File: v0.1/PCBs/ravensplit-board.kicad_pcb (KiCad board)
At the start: 2 copper layers, 131.3 x 100.3 mm, 47 parts

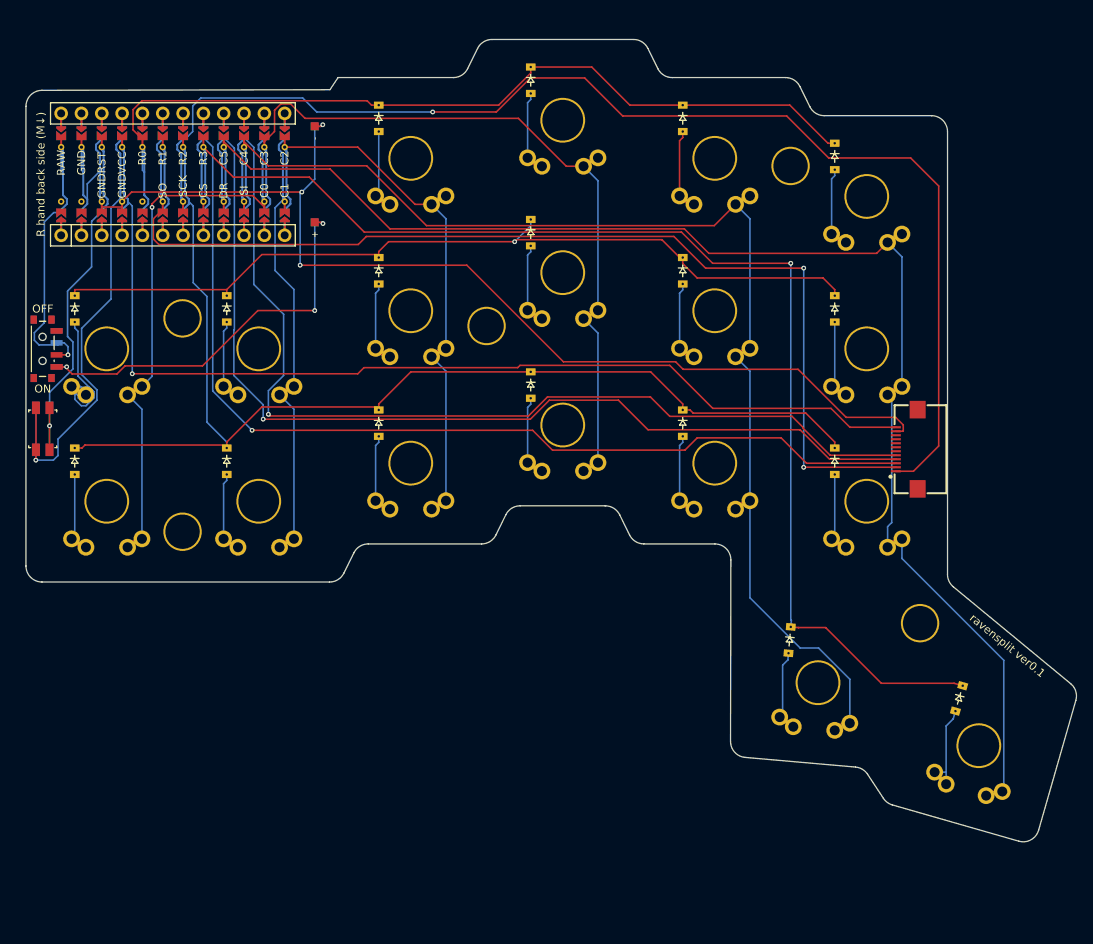
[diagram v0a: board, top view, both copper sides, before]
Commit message: Center MCU better and auto redo PCBs
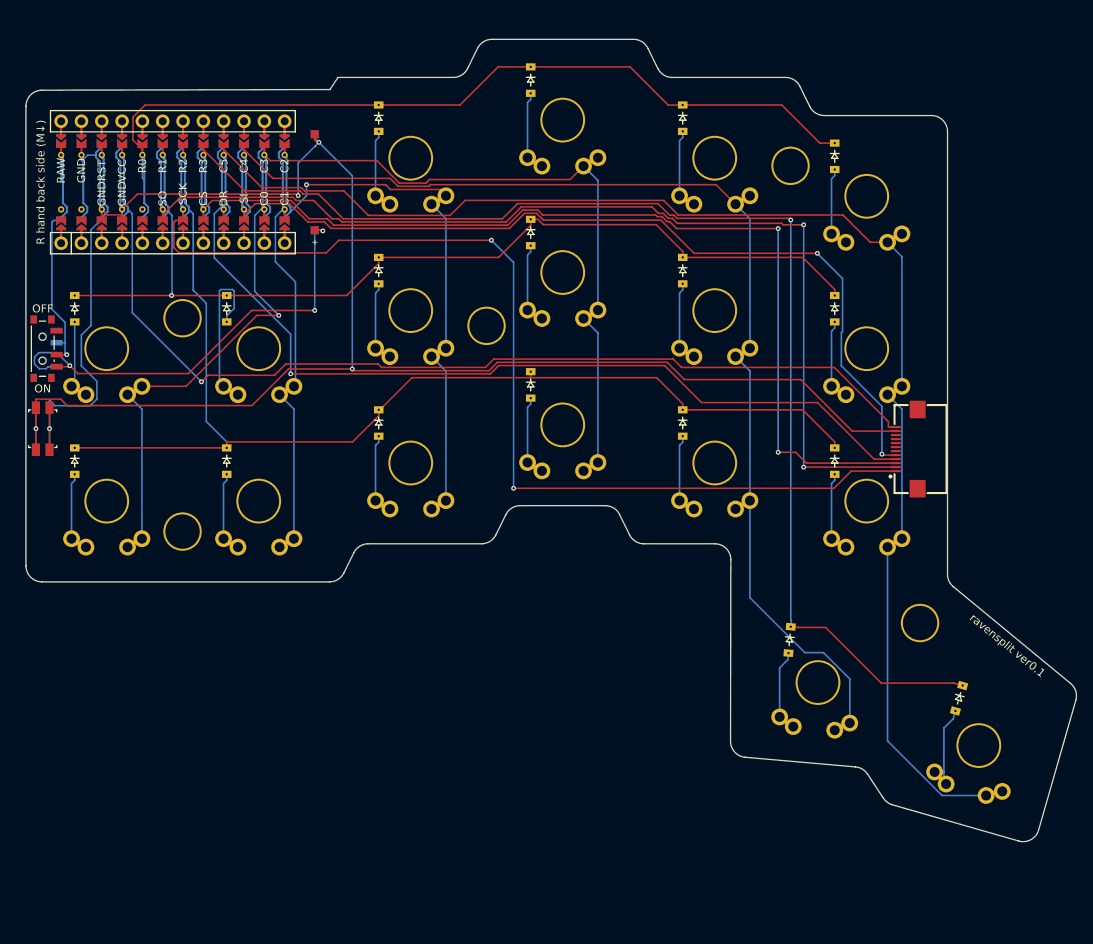
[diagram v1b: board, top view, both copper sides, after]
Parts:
- moved MCU1 0.98 mm to (88.0, 84.5)
- moved PAD1 0.98 mm to (107.0, 90.5)
- moved PAD2 0.98 mm to (107.0, 78.5)
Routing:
- net SCK: track 156.0 -> 136.4 mm, vias 1 -> 2
- net DR: track 130.9 -> 116.7 mm
- net SI: track 130.5 -> 117.2 mm, vias 1 -> 2
- net outer_home: track 23.4 -> 10.5 mm
- net pinky_home: track 10.5 -> 20.6 mm
- net R1: track 117.7 -> 125.8 mm
- net BAT_P: track 50.6 -> 57.4 mm
- net RAW: track 38.6 -> 33.9 mm
- net R3: track 159.9 -> 164.4 mm
- net CS: track 133.1 -> 129.1 mm, vias 1 -> 2
- net RST: track 48.9 -> 52.8 mm
- net C3: track 101.3 -> 97.6 mm
- net VCC: track 131.3 -> 128.1 mm
- net GND: track 222.1 -> 224.9 mm
- net C4: track 158.2 -> 155.5 mm
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
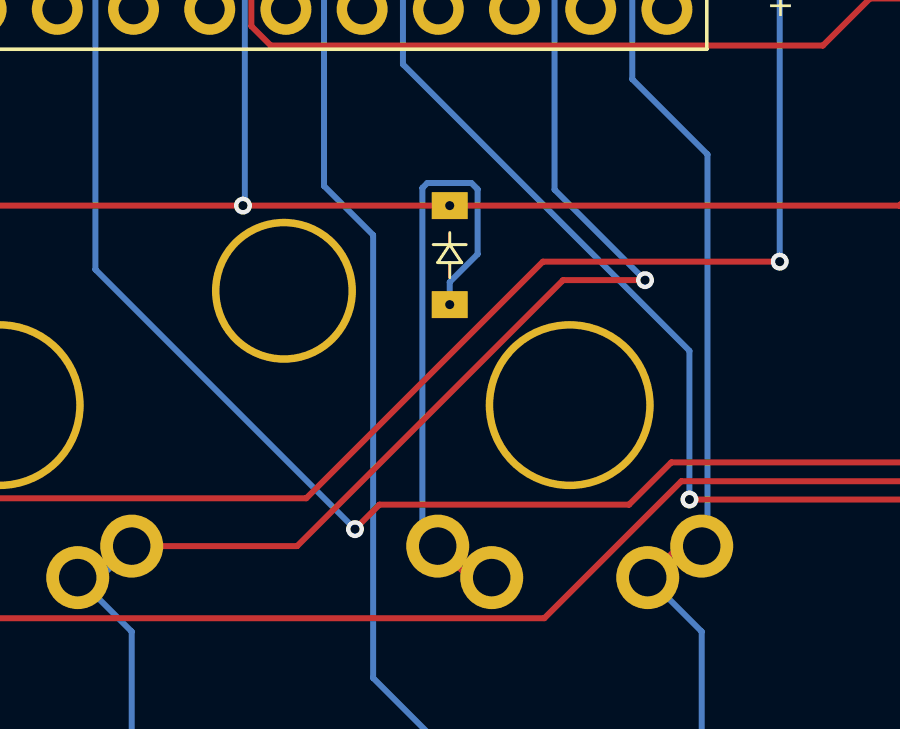
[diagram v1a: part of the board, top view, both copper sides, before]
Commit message: Fix ugly route around diode
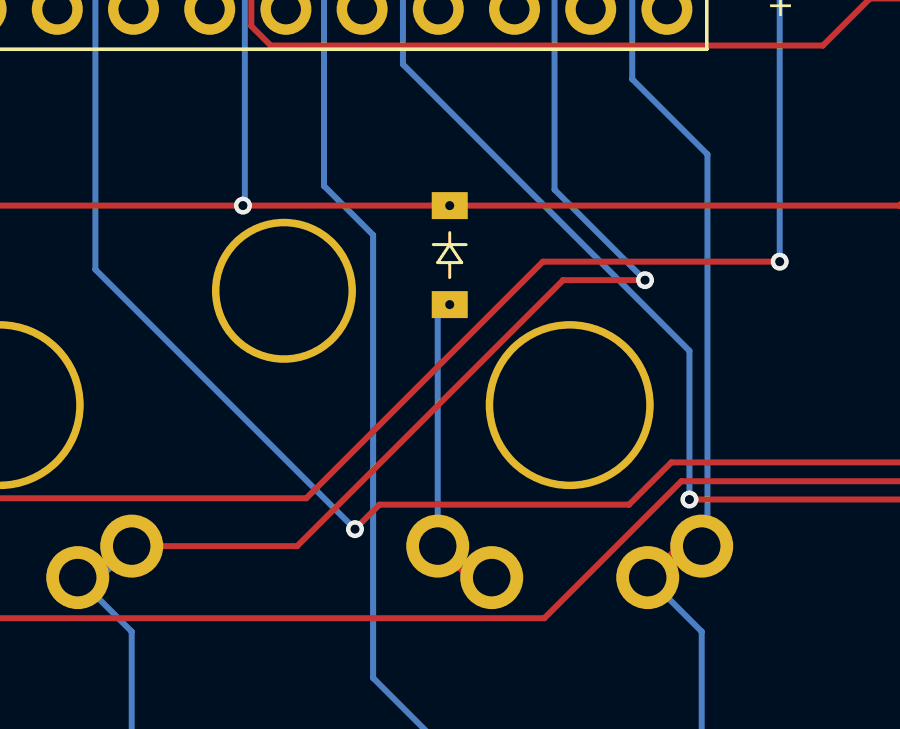
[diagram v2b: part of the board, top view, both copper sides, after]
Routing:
- net pinky_home: track 20.6 -> 11.2 mm
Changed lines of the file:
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@@
 	)
 	(segment
-		(start 95.0944 109.5303)
-		(end 95.0944 98.1033)
-		(width 0.2)
-		(layer "B.Cu")
-		(net 7)
-	)
-	(segment
-		(start 96.7289 97.9378)
-		(end 96.9357 98.1446)
-		(width 0.2)
-		(layer "B.Cu")
-		(net 7)
-	)
-	(segment
-		(start 96.9357 98.1446)
-		(end 96.9357 100.3095)
-		(width 0.2)
-		(layer "B.Cu")
-		(net 7)
-	)
-	(segment
-		(start 95.2599 97.9378)
-		(end 96.7289 97.9378)
-		(width 0.2)
-		(layer "B.Cu")
-		(net 7)
-	)
-	(segment
-		(start 96.0055 101.9914)
-		(end 96.0055 101.2397)
-		(width 0.2)
-		(layer "B.Cu")
-		(net 7)
-	)
-	(segment
-		(start 96.9357 100.3095)
-		(end 96.0055 101.2397)
-		(width 0.2)
-		(layer "B.Cu")
-		(net 7)
-	)
-	(segment
-		(start 95.0944 98.1033)
-		(end 95.2599 97.9378)
+		(start 95.605499 110.0414)
+		(end 95.605499 102.391402)
 		(width 0.2)
 		(layer "B.Cu")
@@
 		(width 0.2)
 		(layer "B.Cu")
+		(net 7)
+	)
+	(segment
+		(start 95.605499 102.391402)
+		(end 96.005501 101.9914)
+		(width 0.2)
+		(layer "B.Cu")

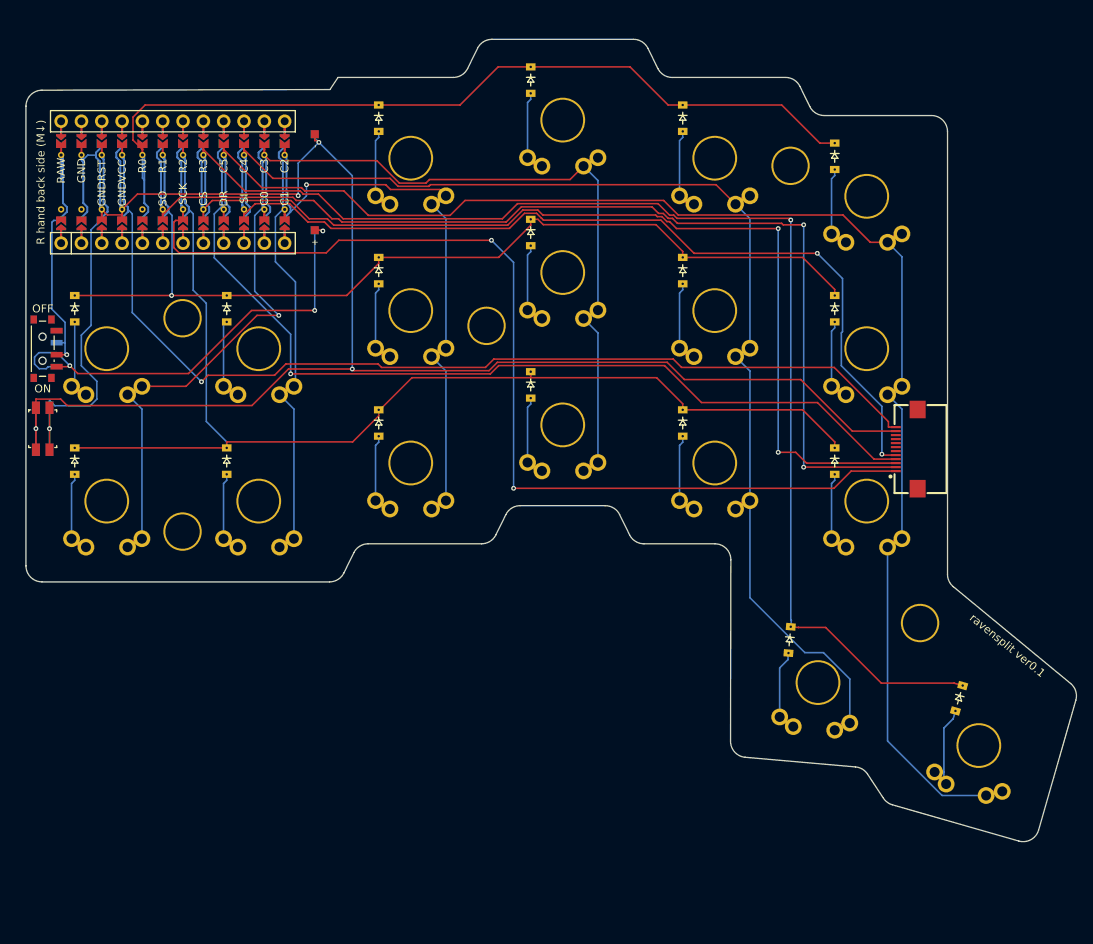
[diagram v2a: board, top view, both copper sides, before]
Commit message: Fix FFC connector orientation
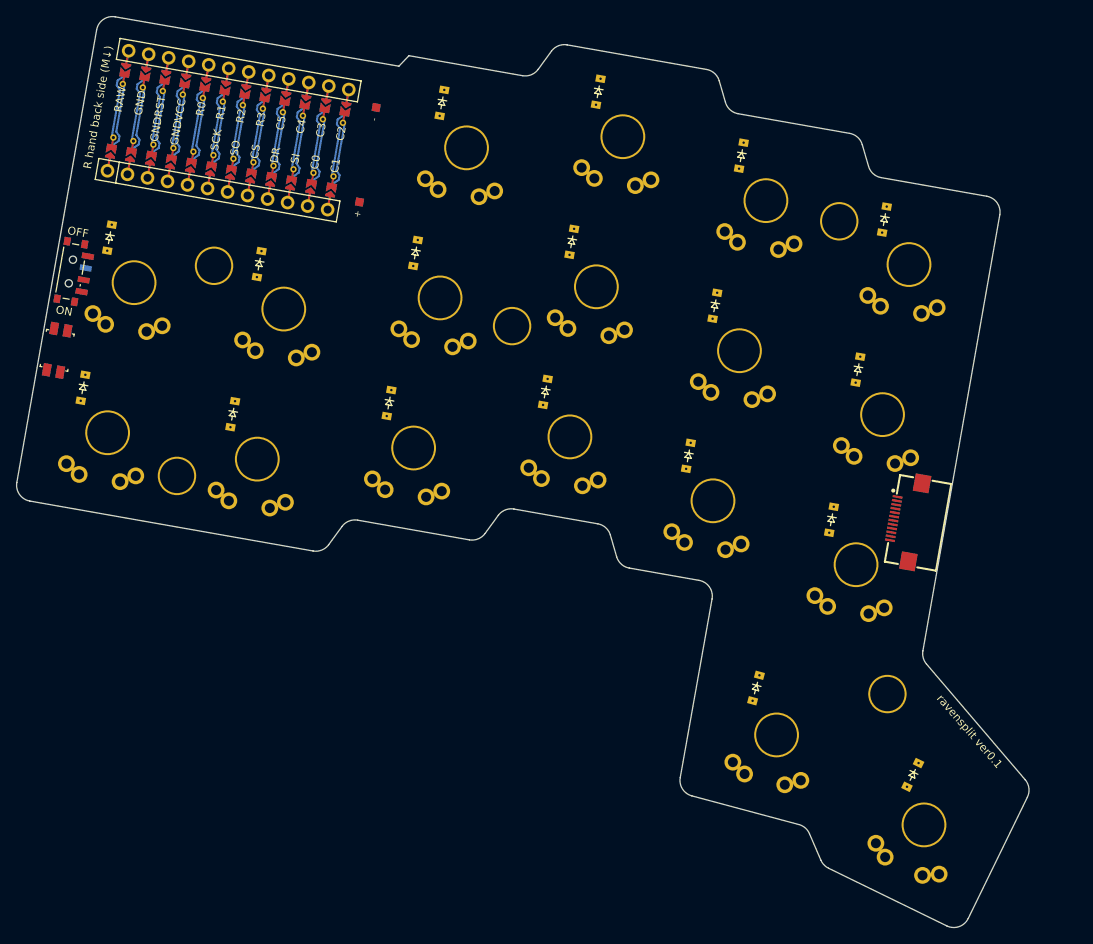
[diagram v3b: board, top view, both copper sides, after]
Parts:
- moved S17 12.1 mm to (183.2, 164.9), turned to -26 degrees
- moved D17 11.2 mm to (181.8, 158.6), turned to -116 degrees
- moved PWR1 10.3 mm to (76.5, 95.7), turned to 170 degrees
- moved D16 10.1 mm to (178.2, 89.2), turned to -100 degrees
- moved S16 10.0 mm to (181.3, 94.8), turned to -10 degrees
- moved RST1 9.96 mm to (74.8, 105.5), turned to 80 degrees
- moved D2 9.88 mm to (81.4, 91.5), turned to -100 degrees
- moved MH2 9.77 mm to (178.6, 148.5), turned to -10 degrees
- moved MCU1 9.65 mm to (94.9, 77.8), turned to 80 degrees
- moved MH1 9.23 mm to (172.6, 89.4), turned to -10 degrees
- moved D1 9.22 mm to (78.0, 110.2), turned to -100 degrees
- moved S2 8.94 mm to (84.4, 97.1), turned to -10 degrees
- moved FFC1 8.92 mm to (180.7, 126.8), turned to 80 degrees
- moved D13 8.70 mm to (160.3, 81.2), turned to -100 degrees
- moved D10 8.57 mm to (142.4, 73.2), turned to -100 degrees
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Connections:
- MCU1 pad 118: SCK -> SO
- MCU1 pad 119: SO -> SCK
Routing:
- net (no net): track 0.00 -> 337.7 mm
- net GND: track 224.9 -> 0.00 mm, vias 4 -> 0
- net C5: track 185.4 -> 0.00 mm
- net R3: track 164.4 -> 0.00 mm, vias 1 -> 0
- net C4: track 155.5 -> 0.00 mm
- net R2: track 147.1 -> 0.00 mm
- net SCK: track 136.4 -> 0.00 mm, vias 2 -> 0
- net SO: track 136.4 -> 0.00 mm, vias 2 -> 0
- net CS: track 129.1 -> 0.00 mm, vias 2 -> 0
- net VCC: track 128.1 -> 0.00 mm, vias 1 -> 0
- net R1: track 125.8 -> 0.00 mm, vias 1 -> 0
- net SI: track 117.2 -> 0.00 mm, vias 2 -> 0
- net DR: track 116.7 -> 0.00 mm, vias 1 -> 0
- net R0: track 111.8 -> 0.00 mm
- net C3: track 97.6 -> 0.00 mm
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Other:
- board size 131.3 x 100.3 mm -> 126.6 x 113.9 mm

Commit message: Add correct routed PCB with DRC ran
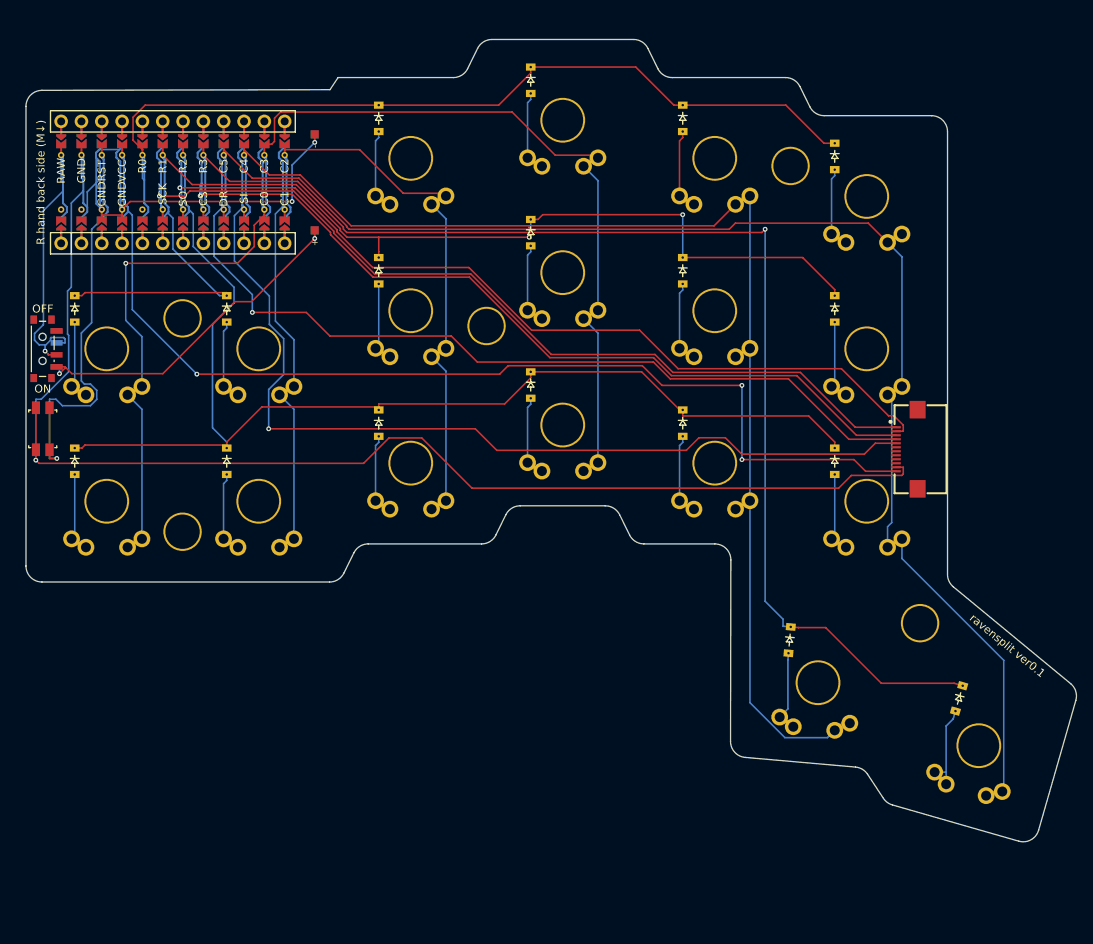
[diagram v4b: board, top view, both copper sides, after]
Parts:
- moved S17 12.0 mm to (190.0, 155.0), turned to -16 degrees
- moved D17 11.2 mm to (187.5, 149.1), turned to -106 degrees
- moved PWR1 10.3 mm to (73.0, 105.4), turned to 180 degrees
- moved D16 10.0 mm to (172.0, 81.3), turned to -90 degrees
- moved S16 10.0 mm to (176.0, 86.3), turned to 0 degrees
- moved RST1 9.98 mm to (73.0, 115.4), turned to 90 degrees
- moved D2 9.90 mm to (77.0, 100.4), turned to -90 degrees
- moved MH2 9.75 mm to (182.7, 139.6), turned to 0 degrees
- moved MCU1 9.66 mm to (88.0, 84.5), turned to 90 degrees
- moved D1 9.24 mm to (77.0, 119.4), turned to -90 degrees
- moved MH1 9.21 mm to (166.5, 82.5), turned to 0 degrees
- moved S2 8.95 mm to (81.0, 105.4), turned to 0 degrees
- moved FFC1 8.90 mm to (181.0, 117.9), turned to 90 degrees
- moved D13 8.69 mm to (153.0, 76.5), turned to -90 degrees
- moved D10 8.56 mm to (134.0, 71.8), turned to -90 degrees
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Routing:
- net (no net): track 337.7 -> 0.00 mm
- net GND: track 0.00 -> 240.9 mm, vias 0 -> 3
- net C5: track 0.00 -> 183.1 mm
- net C4: track 0.00 -> 162.1 mm
- net R3: track 0.00 -> 161.0 mm, vias 0 -> 1
- net R2: track 0.00 -> 150.1 mm
- net R1: track 0.00 -> 145.0 mm, vias 0 -> 2
- net VCC: track 0.00 -> 133.2 mm, vias 0 -> 3
- net SI: track 0.00 -> 123.4 mm, vias 0 -> 1
- net SCK: track 0.00 -> 116.9 mm, vias 0 -> 1
- net SO: track 0.00 -> 115.4 mm, vias 0 -> 1
- net DR: track 0.00 -> 113.0 mm, vias 0 -> 1
- net R0: track 0.00 -> 112.3 mm
- net CS: track 0.00 -> 111.8 mm, vias 0 -> 1
- net C3: track 0.00 -> 102.1 mm
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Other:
- board size 126.6 x 113.9 mm -> 131.3 x 100.3 mm

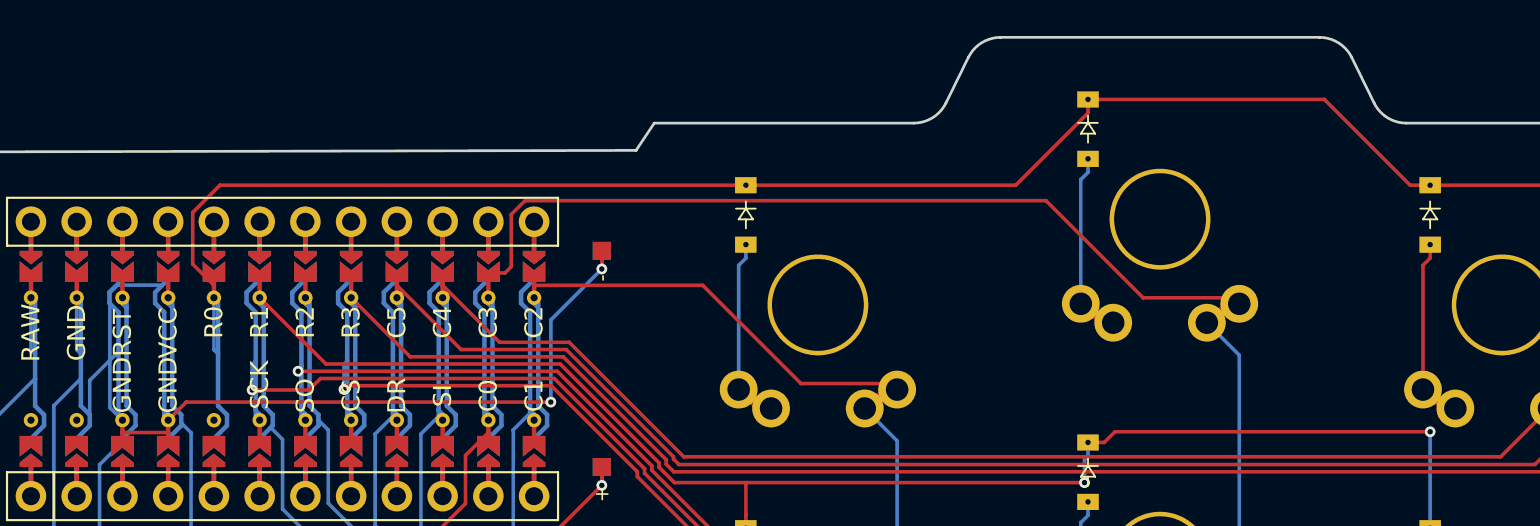
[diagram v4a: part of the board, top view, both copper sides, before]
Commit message: Add text on both sides of PCB
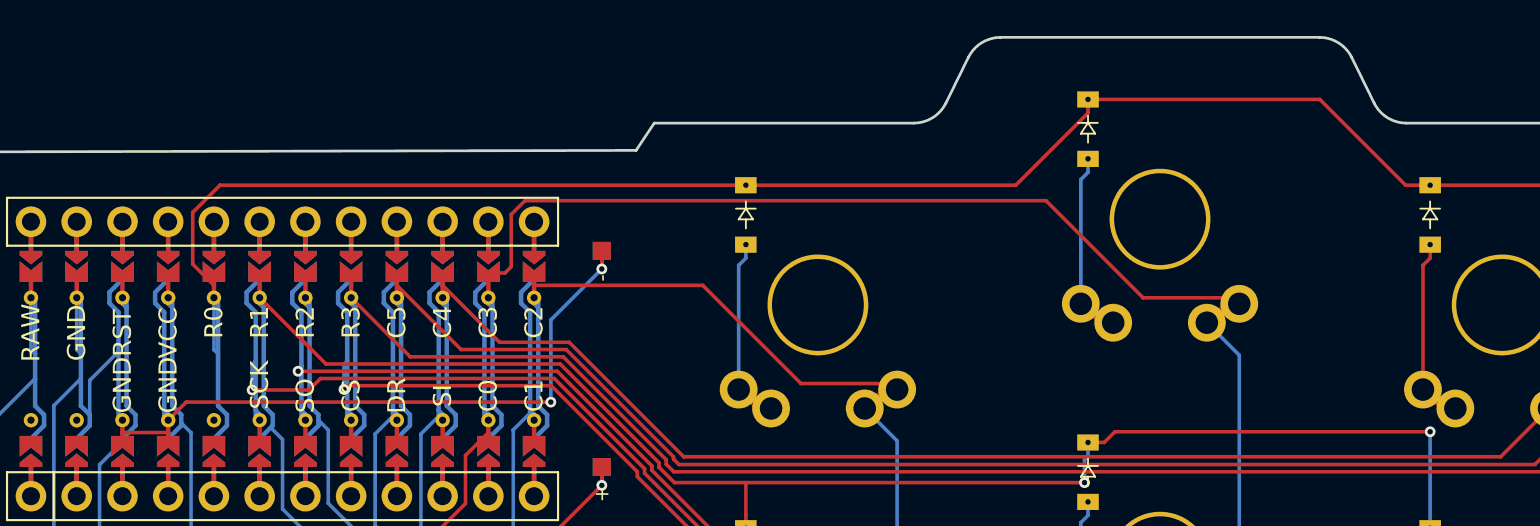
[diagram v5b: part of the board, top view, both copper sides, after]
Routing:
- net GND: track 240.9 -> 230.8 mm
